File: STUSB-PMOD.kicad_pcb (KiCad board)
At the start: 4 copper layers, 26.4 x 16.2 mm, 15 parts, among them J1 Conn_02x06_Odd_Even, J2 dnp, J3 USB_B_Micro, J4 dnp, U1 STUSB03EQ

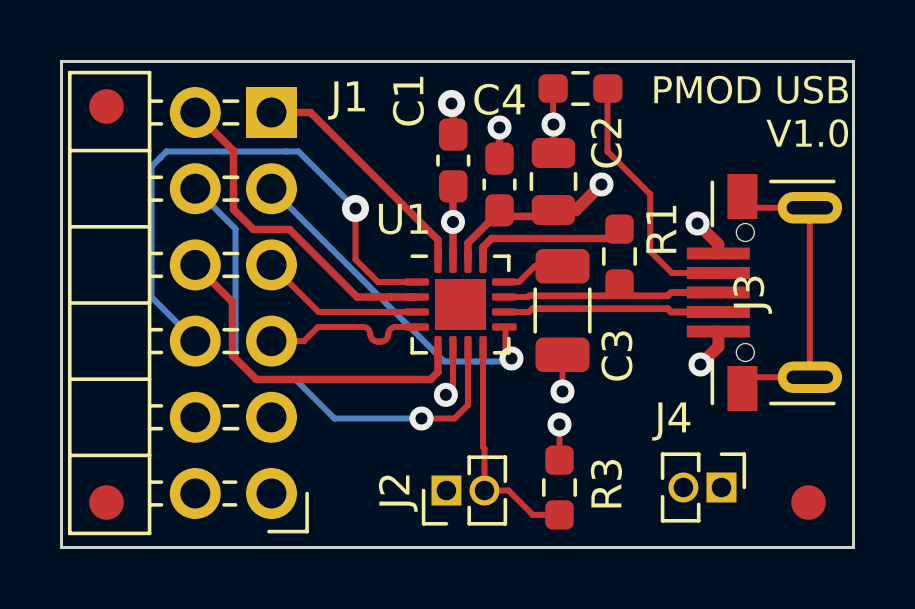
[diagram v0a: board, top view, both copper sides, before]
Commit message: Move C3 to improve solderability
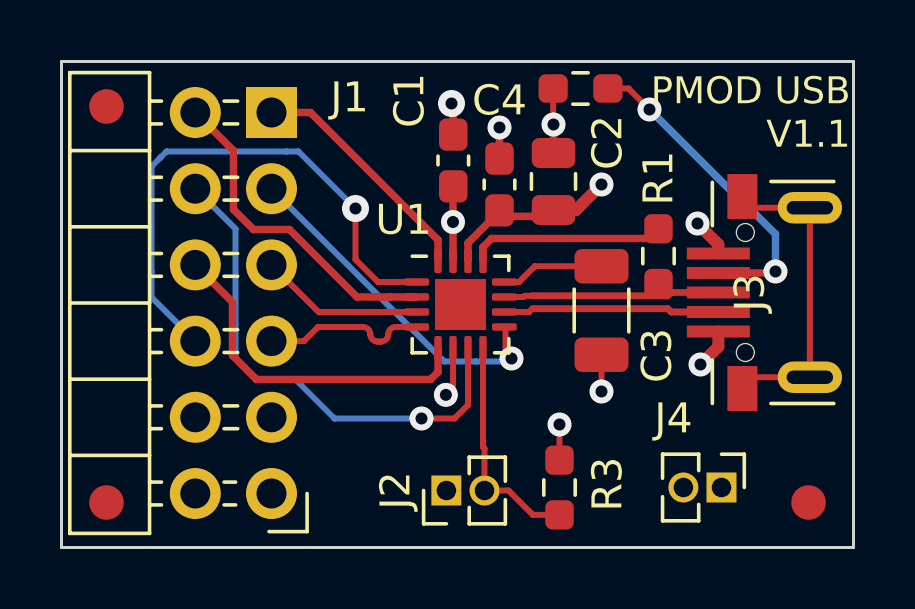
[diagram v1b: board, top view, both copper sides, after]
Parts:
- moved R1 1.30 mm to (141.1, 95.1)
- moved C3 1.30 mm to (139.2, 96.9)
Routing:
- net Net-(J3-Pad4): track 8.59 -> 10.8 mm, vias 0 -> 2
- net Net-(R1-Pad1): track 5.25 -> 6.55 mm
- net Net-(C3-Pad1): track 2.15 -> 3.45 mm
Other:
- board text added: "PMOD USB V1.1"
- board text removed: "PMOD USB V1.0"
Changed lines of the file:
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@@
   (net 19 "Net-(J2-Pad2)")
   (footprint "Resistor_SMD:R_0603_1608Metric_Pad0.98x0.95mm_HandSolder" (layer "F.Cu")
-    (at 139.8 95.1 -90)
+    (at 141.1 95.0875 -90)
     (descr "Resistor SMD 0603 (1608 Metric), square (rectangular) end terminal, IPC_7351 nominal with elongated pad for handsoldering. (Body size source: IPC-SM-782 page 72, https://www.pcb-3d.com/wordpress/wp-content/uploads/ipc-sm-782a_amendment_1_and_2.pdf), generated with kicad-footprint-generator")
     (tags "resistor handsolder")
@@
     (property "Sheetname" "")
     (attr smd)
-    (fp_text reference "R1" (at -0.9 -1.43 90) (layer "F.SilkS")
+    (fp_text reference "R1" (at -2.6 0 90) (layer "F.SilkS")
       (effects (font (size 1 1) (thickness 0.15)))
     )
@@
   )
   (footprint "Capacitor_SMD:C_1206_3216Metric" (layer "F.Cu")
-    (at 137.9 96.9 -90)
+    (at 139.2 96.9 -90)
     (descr "Capacitor SMD 1206 (3216 Metric), square (rectangular) end terminal, IPC_7351 nominal, (Body size source: IPC-SM-782 page 76, https://www.pcb-3d.com/wordpress/wp-content/uploads/ipc-sm-782a_amendment_1_and_2.pdf), generated with kicad-footprint-generator")
     (tags "capacitor")
@@
   )
   (gr_rect (start 121.2 88.6) (end 147.6 104.8) (layer "Edge.Cuts") (width 0.1) (fill none))
-  (gr_text "PMOD USB\nV1.0" (at 147.5 90.3) (layer "F.SilkS")
+  (gr_text "PMOD USB\nV1.1" (at 147.5 90.3) (layer "F.SilkS")
     (effects (font (size 0.9 0.9) (thickness 0.2)) (justify right))
   )
@@
   (via (at 134.25 93.95) (size 0.8) (drill 0.4) (layers "F.Cu" "B.Cu") (net 1))
   (segment (start 135.8 92.0375) (end 135.8 90.8) (width 0.25) (layer "F.Cu") (net 2))
-  (segment (start 137.9 98.375) (end 137.9 99.6) (width 0.2) (layer "F.Cu") (net 2))
+  (segment (start 139.2 98.375) (end 139.2 99.6) (width 0.2) (layer "F.Cu") (net 2))
   (segment (start 134.012299 99.712299) (end 134.25 99.474598) (width 0.2) (layer "F.Cu") (net 2))
   (segment (start 137.6 91.85) (end 137.6 90.7) (width 0.25) (layer "F.Cu") (net 2))
@@
   (via (at 137.8 100.7) (size 0.8) (drill 0.4) (layers "F.Cu" "B.Cu") (net 2))
   (via (at 142.4 94) (size 0.8) (drill 0.4) (layers "F.Cu" "B.Cu") (net 2))
-  (via (at 137.9 99.6) (size 0.8) (drill 0.4) (layers "F.Cu" "B.Cu") (net 2))
+  (via (at 139.2 99.6) (size 0.8) (drill 0.4) (layers "F.Cu" "B.Cu") (net 2))
   (via (at 134.2 90) (size 0.9) (drill 0.4) (layers "F.Cu" "B.Cu") (net 2))
   (via (at 135.8 90.8) (size 0.8) (drill 0.4) (layers "F.Cu" "B.Cu") (net 2))
@@
   (segment (start 135.9625 95.95) (end 136.45 95.95) (width 0.2) (layer "F.Cu") (net 4))
   (segment (start 136.45 95.95) (end 136.975 95.425) (width 0.2) (layer "F.Cu") (net 4))
-  (segment (start 136.975 95.425) (end 137.9 95.425) (width 0.2) (layer "F.Cu") (net 4))
+  (segment (start 136.975 95.425) (end 139.2 95.425) (width 0.2) (layer "F.Cu") (net 4))
   (segment (start 133.75 94.55) (end 133.75 95.2375) (width 0.25) (layer "F.Cu") (net 5))
   (segment (start 129.5 90.3) (end 133.75 94.55) (width 0.25) (layer "F.Cu") (net 5))
@@
   (segment (start 141.408999 96.839) (end 136.89322 96.839) (width 0.228) (layer "F.Cu") (net 13))
   (segment (start 136.78222 96.95) (end 136.89322 96.839) (width 0.2) (layer "F.Cu") (net 13))
+  (segment (start 136.639 96.411) (end 136.6 96.45) (width 0.2) (layer "F.Cu") (net 14))
   (segment (start 141.408999 96.411) (end 136.89322 96.411) (width 0.228) (layer "F.Cu") (net 14))
+  (segment (start 136.6 96.45) (end 135.9625 96.45) (width 0.2) (layer "F.Cu") (net 14))
   (segment (start 143.095 96.3) (end 141.519999 96.3) (width 0.228) (layer "F.Cu") (net 14))
   (segment (start 136.89322 96.411) (end 136.88222 96.4) (width 0.2) (layer "F.Cu") (net 14))
   (segment (start 141.519999 96.3) (end 141.408999 96.411) (width 0.228) (layer "F.Cu") (net 14))
-  (segment (start 135.9625 96.45) (end 136.75 96.45) (width 0.2) (layer "F.Cu") (net 14))
-  (segment (start 136.75 96.45) (end 136.8 96.4) (width 0.2) (layer "F.Cu") (net 14))
-  (segment (start 136.88222 96.4) (end 136.8 96.4) (width 0.2) (layer "F.Cu") (net 14))
-  (segment (start 141.55 95.65) (end 140.825 94.925) (width 0.2) (layer "F.Cu") (net 15))
-  (segment (start 140.825 93.025) (end 139.4 91.6) (width 0.2) (layer "F.Cu") (net 15))
-  (segment (start 143.095 95.65) (end 141.55 95.65) (width 0.2) (layer "F.Cu") (net 15))
+  (segment (start 136.89322 96.411) (end 136.639 96.411) (width 0.2) (layer "F.Cu") (net 14))
+  (segment (start 139.4125 89.5) (end 140.1 89.5) (width 0.2) (layer "F.Cu") (net 15))
+  (segment (start 143.095 95.65) (end 144.95 95.65) (width 0.25) (layer "F.Cu") (net 15))
+  (segment (start 144.95 95.65) (end 145 95.6) (width 0.25) (layer "F.Cu") (net 15))
+  (segment (start 140.1 89.5) (end 140.8 90.2) (width 0.2) (layer "F.Cu") (net 15))
   (segment (start 139.4 89.5125) (end 139.4125 89.5) (width 0.2) (layer "F.Cu") (net 15))
-  (segment (start 139.4 91.6) (end 139.4 89.5125) (width 0.2) (layer "F.Cu") (net 15))
-  (segment (start 140.825 94.925) (end 140.825 93.025) (width 0.2) (layer "F.Cu") (net 15))
+  (via (at 140.8 90.2) (size 0.8) (drill 0.4) (layers "F.Cu" "B.Cu") (net 15))
+  (via (at 145 95.6) (size 0.8) (drill 0.4) (layers "F.Cu" "B.Cu") (net 15))
+  (segment (start 143.8 93.2) (end 140.8 90.2) (width 0.25) (layer "B.Cu") (net 15))
+  (segment (start 145 94.350404) (end 143.849596 93.2) (width 0.25) (layer "B.Cu") (net 15))
+  (segment (start 143.849596 93.2) (end 143.8 93.2) (width 0.25) (layer "B.Cu") (net 15))
+  (segment (start 145 95.6) (end 145 94.350404) (width 0.25) (layer "B.Cu") (net 15))
   (segment (start 146.145 93.475) (end 146.145 99.125) (width 0.2) (layer "F.Cu") (net 16))
   (segment (start 144.27 93.475) (end 143.895 93.1) (width 0.2) (layer "F.Cu") (net 16))
@@
   (segment (start 146.145 99.125) (end 144.27 99.125) (width 0.2) (layer "F.Cu") (net 16))
   (segment (start 146.145 93.475) (end 144.27 93.475) (width 0.2) (layer "F.Cu") (net 16))
-  (segment (start 135.536396 94.5) (end 139.4875 94.5) (width 0.25) (layer "F.Cu") (net 17))
-  (segment (start 139.4875 94.5) (end 139.8 94.1875) (width 0.25) (layer "F.Cu") (net 17))
+  (segment (start 135.25 94.786396) (end 135.536396 94.5) (width 0.25) (layer "F.Cu") (net 17))
   (segment (start 135.25 95.2375) (end 135.25 94.786396) (width 0.25) (layer "F.Cu") (net 17))
-  (segment (start 135.25 94.786396) (end 135.536396 94.5) (width 0.25) (layer "F.Cu") (net 17))
+  (segment (start 140.775 94.5) (end 141.1 94.175) (width 0.25) (layer "F.Cu") (net 17))
+  (segment (start 135.536396 94.5) (end 140.775 94.5) (width 0.25) (layer "F.Cu") (net 17))
   (segment (start 135.25 101.45) (end 135.3 101.5) (width 0.2) (layer "F.Cu") (net 19))
   (segment (start 136.9125 103.7125) (end 137.8 103.7125) (width 0.2) (layer "F.Cu") (net 19))
